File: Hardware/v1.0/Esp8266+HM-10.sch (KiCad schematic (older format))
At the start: 27 parts, among them P1 USB_A, P2 CONN_02X04, SW1 USER_SW, SW2 RST_SW, SW3 Mode, U1 AMS1117-3V3, U2 ESP-12E, U3 HM-10

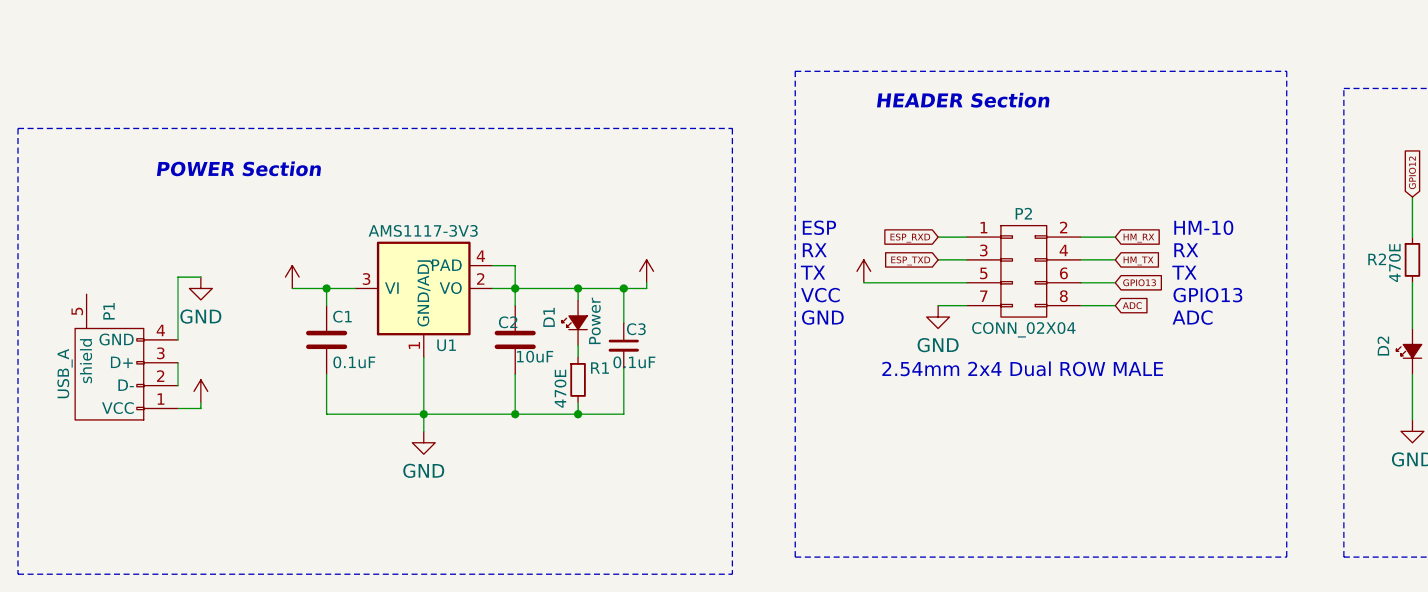
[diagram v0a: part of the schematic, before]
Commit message: Schematic and layout changed
- Schematic
i removed 2x4 header and added 1x5 ,1x4 header
- layout changed
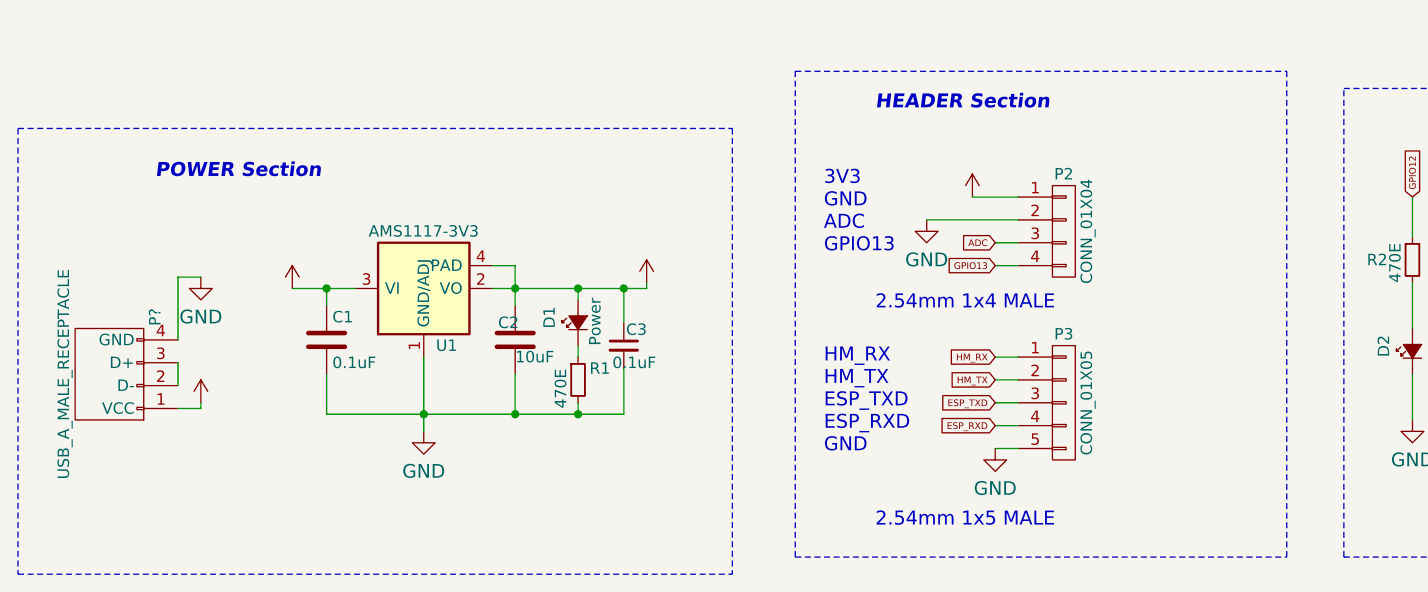
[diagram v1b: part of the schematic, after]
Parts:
- removed P1: USB_A, USB:usb-PCB_male, symbol USB_A
- removed P2: CONN_02X04, Pin_Headers:Pin_Header_Straight_2x04, symbol CONN_02X04
- added P2: CONN_01X04, symbol CONN_01X04
- added P3: CONN_01X05, symbol CONN_01X05
- added P?: USB_A_MALE_RECEPTACLE, symbol USB_A_MALE_RECEPTACLE
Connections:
- net +3V3: now also P2.1 (P1)
- net +5V: now also P?.1 (VCC)
- net ADC: now also P2.3 (P3)
- net ESP_RXD: now also P3.4 (P4)
- net ESP_TXD: now also P3.3 (P3)
- net GND: now also P2.2 (P2), P3.5 (P5), P?.4 (GND)
- net GPIO13: now also P2.4 (P4)
- net HM_RX: now also P3.1 (P1)
- net HM_TX: now also P3.2 (P2)
- new net: P?.2 (D-), P?.3 (D+)
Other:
- note added: "2.54mm 1x4 MALE"
- note added: "2.54mm 1x5 MALE"
- note added: "3V3\nGND\nADC\nGPIO13"
- note added: "HM_RX\nHM_TX\nESP_TXD\nESP_RXD\nGND"
- note removed: "2.54mm 2x4 Dual ROW MALE"
- note removed: "ESP\nRX\nTX\nVCC\nGND"
- note removed: "HM-10\nRX\nTX\nGPIO13\nADC"
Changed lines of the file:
@@
 LIBS:valves
 LIBS:ESP8266
-LIBS:HM-10
-LIBS:AMS1117-3V3
-LIBS:usb_a_4_pins
 LIBS:Esp8266+HM-10-cache
 EELAYER 25 0
@@
 $EndComp
 $Comp
-L GND #PWR01
+L GND #PWR5
 U 1 1 58484B9B
 P 2700 5675
-F 0 "#PWR01" H 2700 5725 30  0001 C CNN
+F 0 "#PWR5" H 2700 5725 30  0001 C CNN
 F 1 "GND" H 2700 5550 30  0001 C CNN
 F 2 "GND" H 2700 5500 60  0000 C CNN
@@
 $EndComp
 $Comp
-L +3V3 #PWR02
+L +3V3 #PWR6
 U 1 1 58485B69
 P 3675 5025
-F 0 "#PWR02" H 3675 5250 30  0001 C CNN
+F 0 "#PWR6" H 3675 5250 30  0001 C CNN
 F 1 "+3V3" V 3600 5025 30  0001 C CNN
 F 2 "" H 3675 5025 60  0000 C CNN
@@
 $EndComp
 $Comp
-L +5V #PWR03
+L +5V #PWR3
 U 1 1 58485ED1
 P 2125 5050
-F 0 "#PWR03" H 2125 5275 30  0001 C CNN
+F 0 "#PWR3" H 2125 5275 30  0001 C CNN
 F 1 "+5V" V 2050 5050 30  0001 C CNN
 F 2 "" H 2125 5050 60  0000 C CNN
@@
 ESP_TXD
 $Comp
-L GND #PWR04
+L GND #PWR4
 U 1 1 58487185
 P 2300 2000
-F 0 "#PWR04" H 2300 2050 30  0001 C CNN
+F 0 "#PWR4" H 2300 2050 30  0001 C CNN
 F 1 "GND" H 2300 1875 30  0001 C CNN
 F 2 "GND" H 2300 1825 60  0000 C CNN
@@
 $EndComp
 $Comp
-L GND #PWR05
+L GND #PWR17
 U 1 1 58489C98
 P 8400 5625
-F 0 "#PWR05" H 8400 5675 30  0001 C CNN
+F 0 "#PWR17" H 8400 5675 30  0001 C CNN
 F 1 "GND" H 8400 5500 30  0001 C CNN
 F 2 "GND" H 8400 5450 60  0000 C CNN
@@
 $EndComp
 $Comp
-L +3V3 #PWR06
+L +3V3 #PWR16
 U 1 1 5848B492
 P 8400 4950
-F 0 "#PWR06" H 8400 5175 30  0001 C CNN
+F 0 "#PWR16" H 8400 5175 30  0001 C CNN
 F 1 "+3V3" V 8325 4950 30  0001 C CNN
 F 2 "" H 8400 4950 60  0000 C CNN
@@
 GPIO0
 $Comp
-L +3V3 #PWR07
+L +3V3 #PWR20
 U 1 1 584914E0
 P 9300 5600
-F 0 "#PWR07" H 9300 5825 30  0001 C CNN
+F 0 "#PWR20" H 9300 5825 30  0001 C CNN
 F 1 "+3V3" V 9225 5600 30  0001 C CNN
 F 2 "" H 9300 5600 60  0000 C CNN
@@
 $EndComp
 $Comp
-L GND #PWR08
+L GND #PWR18
 U 1 1 5849196E
 P 8975 5650
-F 0 "#PWR08" H 8975 5700 30  0001 C CNN
+F 0 "#PWR18" H 8975 5700 30  0001 C CNN
 F 1 "GND" H 8975 5525 30  0001 C CNN
 F 2 "GND" H 8975 5475 60  0000 C CNN
@@
 $EndComp
 $Comp
-L +3V3 #PWR09
+L +3V3 #PWR21
 U 1 1 584939F4
 P 9650 4900
-F 0 "#PWR09" H 9650 5125 30  0001 C CNN
+F 0 "#PWR21" H 9650 5125 30  0001 C CNN
 F 1 "+3V3" V 9575 4900 30  0001 C CNN
 F 2 "" H 9650 4900 60  0000 C CNN
@@
 HM_TX
 $Comp
-L +3V3 #PWR012
+L +3V3 #PWR7
 U 1 1 5849EA39
 P 4675 2000
-F 0 "#PWR012" H 4675 2225 30  0001 C CNN
+F 0 "#PWR7" H 4675 2225 30  0001 C CNN
 F 1 "+3V3" V 4600 2000 30  0001 C CNN
 F 2 "" H 4675 2000 60  0000 C CNN
@@
 Text GLabel 4650 2300 2    29   Input ~ 0
 GPIO14
-Text GLabel 4950 4925 0    29   Input ~ 0
+Text GLabel 5200 5550 0    29   Input ~ 0
 ESP_TXD
-Text GLabel 4950 4825 0    29   Input ~ 0
-ESP_RXD
-$Comp
-L GND #PWR013
-U 1 1 584A5D79
-P 4950 5125
-F 0 "#PWR013" H 4950 5175 30  0001 C CNN
-F 1 "GND" H 4950 5000 30  0001 C CNN
-F 2 "GND" H 4950 4950 60  0000 C CNN
-F 3 "" H 4950 5125 60  0000 C CNN
-	1    4950 5125
-	1    0    0    -1
-$EndComp
+Text GLabel 5200 5350 0    29   Input ~ 0
+HM_RX
 Text GLabel 6800 1500 0    29   Input ~ 0
 HM_TX
@@
 HM_RX
 $Comp
-L +3V3 #PWR014
+L +3V3 #PWR11
 U 1 1 584ADBF1
 P 6250 2500
-F 0 "#PWR014" H 6250 2725 30  0001 C CNN
+F 0 "#PWR11" H 6250 2725 30  0001 C CNN
 F 1 "+3V3" V 6175 2500 30  0001 C CNN
 F 2 "" H 6250 2500 60  0000 C CNN
@@
 $EndComp
 $Comp
-L GND #PWR015
+L GND #PWR13
 U 1 1 584AF0C5
 P 7300 3375
-F 0 "#PWR015" H 7300 3425 30  0001 C CNN
+F 0 "#PWR13" H 7300 3425 30  0001 C CNN
 F 1 "GND" H 7300 3250 30  0001 C CNN
 F 2 "GND" H 7300 3200 60  0000 C CNN
@@
 $EndComp
 $Comp
-L GND #PWR016
+L GND #PWR19
 U 1 1 584B2D10
 P 9100 2400
-F 0 "#PWR016" H 9100 2450 30  0001 C CNN
+F 0 "#PWR19" H 9100 2450 30  0001 C CNN
 F 1 "GND" H 9100 2275 30  0001 C CNN
 F 2 "GND" H 9100 2225 60  0000 C CNN
@@
 $EndComp
 $Comp
-L +3V3 #PWR017
+L +3V3 #PWR14
 U 1 1 584B99E7
 P 7650 4600
-F 0 "#PWR017" H 7650 4825 30  0001 C CNN
+F 0 "#PWR14" H 7650 4825 30  0001 C CNN
 F 1 "+3V3" V 7575 4600 30  0001 C CNN
 F 2 "" H 7650 4600 60  0000 C CNN
@@
 $EndComp
 $Comp
-L GND #PWR018
+L GND #PWR15
 U 1 1 584BAEE4
 P 7650 5650
-F 0 "#PWR018" H 7650 5700 30  0001 C CNN
+F 0 "#PWR15" H 7650 5700 30  0001 C CNN
 F 1 "GND" H 7650 5525 30  0001 C CNN
 F 2 "GND" H 7650 5475 60  0000 C CNN
@@
 GPIO14
 $Comp
-L +5V #PWR019
+L +5V #PWR2
 U 1 1 584DC01E
 P 1725 5550
-F 0 "#PWR019" H 1725 5775 30  0001 C CNN
+F 0 "#PWR2" H 1725 5775 30  0001 C CNN
 F 1 "+5V" V 1650 5550 30  0001 C CNN
 F 2 "" H 1725 5550 60  0000 C CNN
@@
 $EndComp
 $Comp
-L GND #PWR020
+L GND #PWR1
 U 1 1 584DC622
 P 1725 5000
-F 0 "#PWR020" H 1725 5050 30  0001 C CNN
+F 0 "#PWR1" H 1725 5050 30  0001 C CNN
 F 1 "GND" H 1725 4875 30  0001 C CNN
 F 2 "GND" H 1725 4825 60  0000 C CNN
@@
 Text GLabel 6800 2400 0    29   Input ~ 0
 HM_RESET
-Text GLabel 5725 4825 2    29   Input ~ 0
-HM_RX
-Text GLabel 5725 4925 2    29   Input ~ 0
+Text GLabel 5200 5450 0    29   Input ~ 0
 HM_TX
 $Comp
@@
 $EndComp
 $Comp
-L GND #PWR021
+L GND #PWR12
 U 1 1 584D4B1F
 P 7025 5625
-F 0 "#PWR021" H 7025 5675 30  0001 C CNN
+F 0 "#PWR12" H 7025 5675 30  0001 C CNN
 F 1 "GND" H 7025 5500 30  0001 C CNN
 F 2 "GND" H 7025 5450 60  0000 C CNN
@@
 GPIO12
 $Comp
-L +3V3 #PWR022
+L +3V3 #PWR9
 U 1 1 584D6E8E
-P 4625 5025
-F 0 "#PWR022" H 4625 5250 30  0001 C CNN
-F 1 "+3V3" V 4550 5025 30  0001 C CNN
-F 2 "" H 4625 5025 60  0000 C CNN
-F 3 "" H 4625 5025 60  0000 C CNN
-	1    4625 5025
-	1    0    0    -1
-$EndComp
-$Comp
-L CONN_02X04 P2
-U 1 1 584D7A22
-P 5325 4975
-F 0 "P2" H 5325 5225 50  0000 C CNN
-F 1 "CONN_02X04" H 5325 4725 50  0000 C CNN
-F 2 "Pin_Headers:Pin_Header_Straight_2x04" H 5325 3775 50  0001 C CNN
-F 3 "" H 5325 3775 50  0000 C CNN
-	1    5325 4975
-	1    0    0    -1
-$EndComp
-Text GLabel 5725 5025 2    29   Input ~ 0
+P 5100 4650
+F 0 "#PWR9" H 5100 4875 30  0001 C CNN
+F 1 "+3V3" V 5025 4650 30  0001 C CNN
+F 2 "" H 5100 4650 60  0000 C CNN
+F 3 "" H 5100 4650 60  0000 C CNN
+	1    5100 4650
+	1    0    0    -1
+$EndComp
+Text GLabel 5200 4950 0    29   Input ~ 0
 GPIO13
 NoConn ~ 8350 2500
@@
 Text GLabel 4650 2600 2    29   Input ~ 0
 ADC
-Text GLabel 5725 5125 2    29   Input ~ 0
+Text GLabel 5200 4850 0    29   Input ~ 0
 ADC
-Text Notes 4700 5450 0    61   ~ 0
-2.54mm 2x4 Dual ROW MALE
-Text Notes 4350 5225 0    61   ~ 0
-ESP\nRX\nTX\nVCC\nGND
-Text Notes 5975 5225 0    61   ~ 0
-HM-10\nRX\nTX\nGPIO13\nADC
+Text Notes 4675 5150 0    61   ~ 0
+2.54mm 1x4 MALE
+Text Notes 4450 5775 0    61   ~ 0
+HM_RX\nHM_TX\nESP_TXD\nESP_RXD\nGND
 Text GLabel 10725 4875 1    29   Input ~ 0
 GPIO15
@@
 $EndComp
 $Comp
-L GND #PWR023
+L GND #PWR22
 U 1 1 584F045A
 P 10725 5400
-F 0 "#PWR023" H 10725 5450 30  0001 C CNN
+F 0 "#PWR22" H 10725 5450 30  0001 C CNN
 F 1 "GND" H 10725 5275 30  0001 C CNN
 F 2 "GND" H 10725 5225 60  0000 C CNN
@@
 	4525 2300 4650 2300
 Wire Wire Line
-	4950 4825 5075 4825
-Wire Wire Line
-	4950 4925 5075 4925
-Wire Wire Line
-	5075 5125 4950 5125
-Wire Wire Line
-	4625 5025 5075 5025
-Wire Wire Line
 	6800 1400 6950 1400
 Wire Wire Line
@@
 	7025 5625 7025 5425
 Wire Wire Line
-	5725 4925 5575 4925
-Wire Wire Line
-	5575 4825 5725 4825
-Wire Wire Line
-	5725 5025 5575 5025
-Wire Wire Line
-	5575 5125 5725 5125
-Wire Wire Line
 	7025 4650 7025 4825
 Wire Wire Line
@@
 Wire Notes Line
 	11000 4175 10725 4175
-$Comp
-L USB_A P1
-U 1 1 584DA3D8
+Wire Wire Line
+	1625 5000 1725 5000
+Wire Wire Line
+	3000 5050 3675 5050
+$Comp
+L CONN_01X04 P2
+U 1 1 58500377
+P 5500 4800
+F 0 "P2" H 5500 5050 50  0000 C CNN
+F 1 "CONN_01X04" V 5600 4800 50  0000 C CNN
+F 2 "" H 5500 4800 50  0000 C CNN
+F 3 "" H 5500 4800 50  0000 C CNN
+	1    5500 4800
+	1    0    0    -1
+$EndComp
+$Comp
+L CONN_01X05 P3
+U 1 1 58500404
+P 5500 5550
+F 0 "P3" H 5500 5850 50  0000 C CNN
+F 1 "CONN_01X05" V 5600 5550 50  0000 C CNN
+F 2 "" H 5500 5550 50  0000 C CNN
+F 3 "" H 5500 5550 50  0000 C CNN
+	1    5500 5550
+	1    0    0    -1
+$EndComp
+Text GLabel 5200 5650 0    29   Input ~ 0
+ESP_RXD
+$Comp
+L GND #PWR10
+U 1 1 58502BBE
+P 5200 5750
+F 0 "#PWR10" H 5200 5800 30  0001 C CNN
+F 1 "GND" H 5200 5625 30  0001 C CNN
+F 2 "GND" H 5200 5575 60  0000 C CNN
+F 3 "" H 5200 5750 60  0000 C CNN
+	1    5200 5750
+	1    0    0    -1
+$EndComp
+Wire Wire Line
+	5300 5750 5200 5750
+Wire Wire Line
+	5300 5650 5200 5650
+Wire Wire Line
+	5300 5550 5200 5550
+Wire Wire Line
+	5300 5450 5200 5450
+Wire Wire Line
+	5300 5350 5200 5350
+$Comp
+L GND #PWR8
+U 1 1 585036A7
+P 4900 4750
+F 0 "#PWR8" H 4900 4800 30  0001 C CNN
+F 1 "GND" H 4900 4625 30  0001 C CNN
+F 2 "GND" H 4900 4575 60  0000 C CNN
+F 3 "" H 4900 4750 60  0000 C CNN
+	1    4900 4750
+	1    0    0    -1
+$EndComp
+Wire Wire Line
+	5300 4950 5200 4950
+Wire Wire Line
+	5300 4650 5100 4650
+Wire Wire Line
+	4900 4750 5300 4750
+Wire Wire Line
+	5300 4850 5200 4850
+Text Notes 4450 4900 0    61   ~ 0
+3V3\nGND\nADC\nGPIO13
+Text Notes 4675 6100 0    61   ~ 0
+2.54mm 1x5 MALE
+$Comp
+L USB_A_MALE_RECEPTACLE P?
+U 1 1 5851C6B4
 P 1325 5375
-F 0 "P1" H 1550 5375 50  0000 C CNN
-F 1 "USB_A" H 1275 5575 50  0000 C CNN
-F 2 "USB:usb-PCB_male" V 1275 5275 50  0001 C CNN
+F 0 "P?" H 1525 5175 50  0000 C CNN
+F 1 "USB_A_MALE_RECEPTACLE" H 1275 5575 50  0000 C CNN
+F 2 "" V 1275 5275 50  0000 C CNN
 F 3 "" V 1275 5275 50  0000 C CNN
 	1    1325 5375
 	0    -1   -1   0
 $EndComp
-Wire Wire Line
-	1625 5000 1725 5000
-Wire Wire Line
-	3000 5050 3675 5050
 $EndSCHEMATC
